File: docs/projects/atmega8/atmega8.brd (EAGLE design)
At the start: 89.8 x 49.5 mm, 13 parts, among them IC2 MEGA8-P

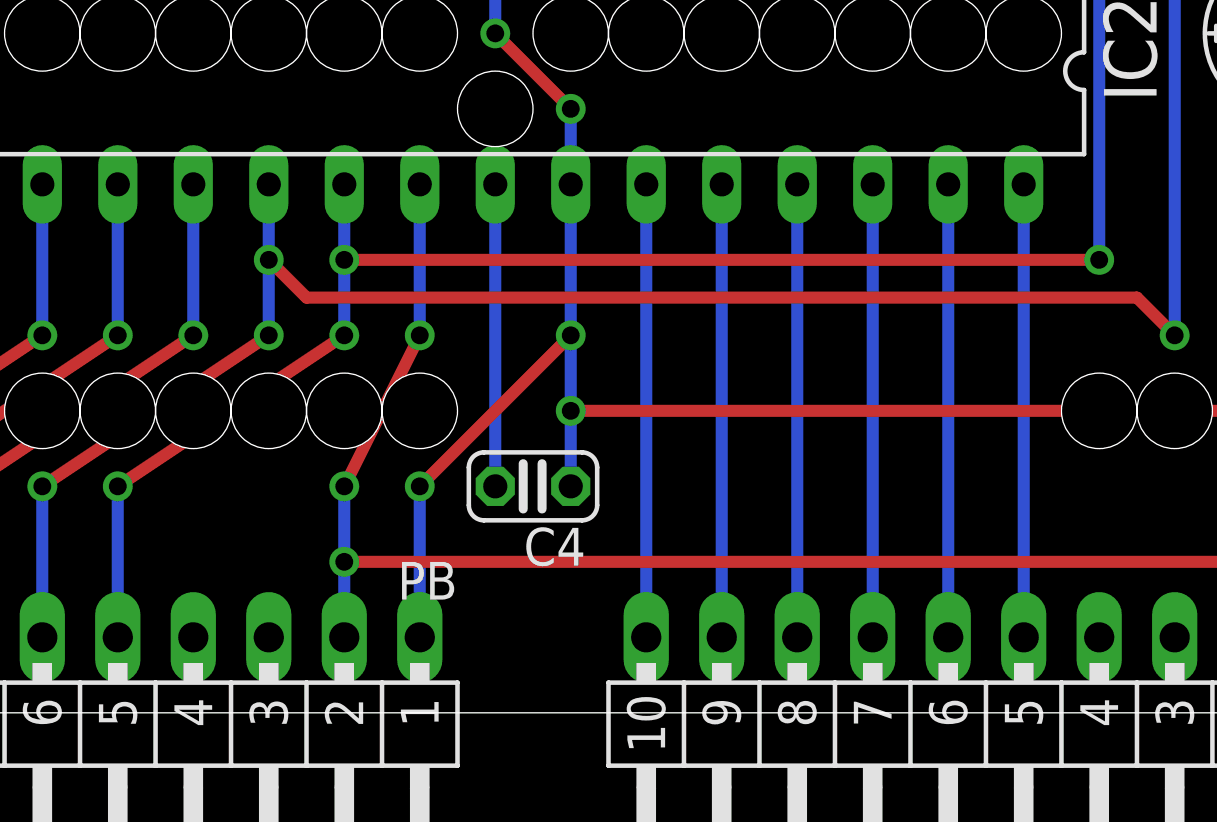
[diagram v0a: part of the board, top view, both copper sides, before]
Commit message: atmega8: 6,7 is connected with 14,15 to make I2C compatible with Nucleo
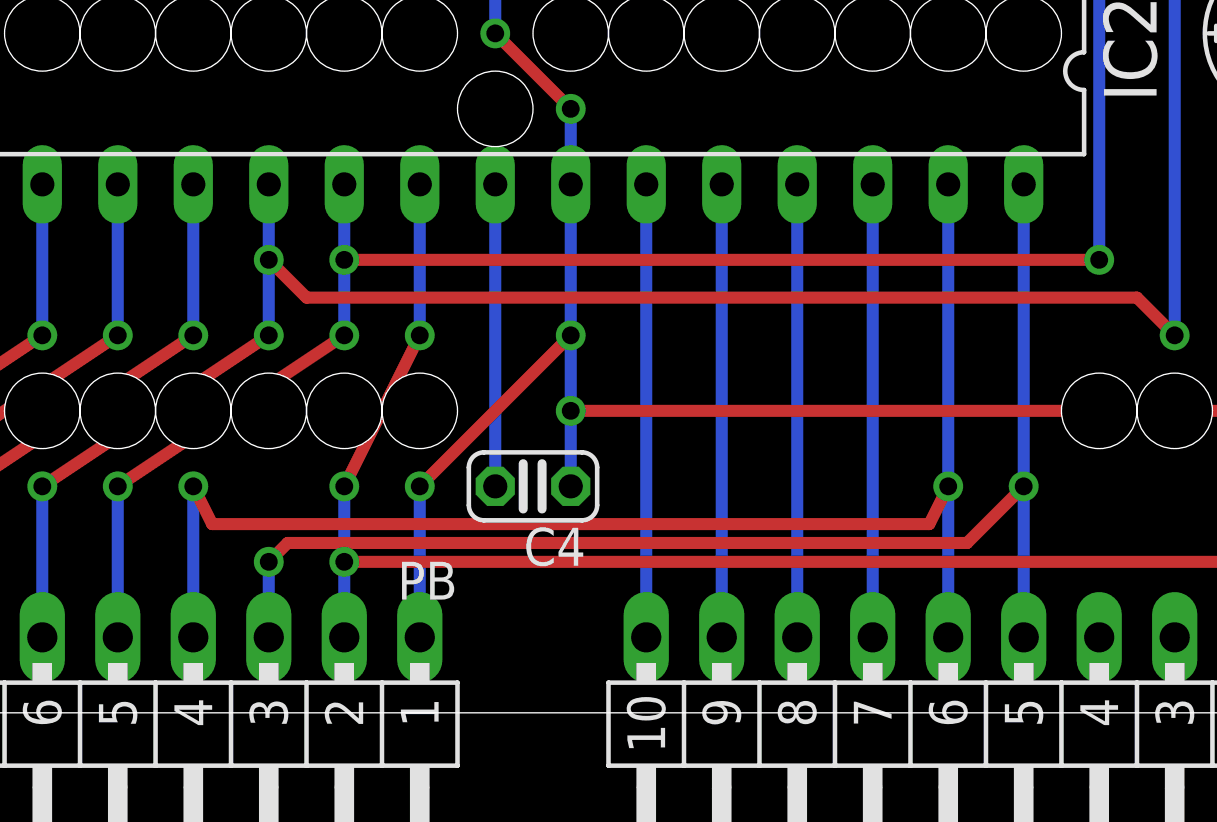
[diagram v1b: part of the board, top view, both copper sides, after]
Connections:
- removed net N$7: IC2.27, PC.6
- removed net N$8: IC2.28, PC.5
- new net A4: IC2.27, PB.4, PC.6
- new net A5: IC2.28, PB.3, PC.5
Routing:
- net A4: track 0.00 -> 47.3 mm, vias 0 -> 2
- net A5: track 0.00 -> 44.2 mm, vias 0 -> 2
- net N$8: track 15.2 -> 0.00 mm
- net N$7: track 15.2 -> 0.00 mm
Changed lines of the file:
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@@
 <?xml version="1.0" encoding="utf-8"?>
 <!DOCTYPE eagle SYSTEM "eagle.dtd">
-<eagle version="6.2">
+<eagle version="7.4.0">
 <drawing>
 <settings>
@@
 <setting verticaltext="up"/>
 </settings>
-<grid distance="0.1" unitdist="inch" unit="inch" style="lines" multiple="1" display="yes" altdistance="0.05" altunitdist="inch" altunit="inch"/>
+<grid distance="0.1" unitdist="inch" unit="inch" style="lines" multiple="1" display="yes" altdistance="0.025" altunitdist="inch" altunit="inch"/>
 <layers>
 <layer number="1" name="Top" color="4" fill="1" visible="yes" active="yes"/>
@@
 </class>
 </classes>
-<designrules>
+<designrules name="default">
 <description language="de">&lt;b&gt;EAGLE Design Rules&lt;/b&gt;
 &lt;p&gt;
@@
 <pass name="Default">
 <param name="RoutingGrid" value="50mil"/>
+<param name="AutoGrid" value="1"/>
+<param name="Efforts" value="0"/>
+<param name="TopRouterVariant" value="1"/>
 <param name="tpViaShape" value="round"/>
 <param name="PrefDir.1" value="|"/>
@@
 <wire x1="40.64" y1="2.54" x2="40.64" y2="17.78" width="0.4064" layer="16"/>
 </signal>
-<signal name="N$7">
+<signal name="A4">
 <contactref element="PC" pad="6"/>
 <contactref element="IC2" pad="27"/>
-<wire x1="43.18" y1="2.54" x2="43.18" y2="17.78" width="0.4064" layer="16"/>
-</signal>
-<signal name="N$8">
+<contactref element="PB" pad="4"/>
+<wire x1="43.18" y1="7.62" x2="43.18" y2="17.78" width="0.4064" layer="16"/>
+<wire x1="43.18" y1="2.54" x2="43.18" y2="7.62" width="0.4064" layer="16"/>
+<via x="43.18" y="7.62" extent="1-16" drill="0.6" shape="square"/>
+<wire x1="43.18" y1="7.62" x2="42.545" y2="6.35" width="0.4064" layer="1"/>
+<wire x1="42.545" y1="6.35" x2="18.415" y2="6.35" width="0.4064" layer="1"/>
+<wire x1="18.415" y1="6.35" x2="17.78" y2="7.62" width="0.4064" layer="1"/>
+<via x="17.78" y="7.62" extent="1-16" drill="0.6" shape="square"/>
+<wire x1="17.78" y1="7.62" x2="17.78" y2="2.54" width="0.4064" layer="16"/>
+</signal>
+<signal name="A5">
 <contactref element="PC" pad="5"/>
 <contactref element="IC2" pad="28"/>
-<wire x1="45.72" y1="2.54" x2="45.72" y2="17.78" width="0.4064" layer="16"/>
+<contactref element="PB" pad="3"/>
+<wire x1="45.72" y1="7.62" x2="45.72" y2="17.78" width="0.4064" layer="16"/>
+<wire x1="45.72" y1="2.54" x2="45.72" y2="7.62" width="0.4064" layer="16"/>
+<via x="45.72" y="7.62" extent="1-16" drill="0.6" shape="square"/>
+<wire x1="45.72" y1="7.62" x2="43.815" y2="5.715" width="0.4064" layer="1"/>
+<via x="20.32" y="5.08" extent="1-16" drill="0.6" shape="square"/>
+<wire x1="20.32" y1="5.08" x2="20.32" y2="2.54" width="0.4064" layer="16"/>
+<wire x1="43.815" y1="5.715" x2="20.955" y2="5.715" width="0.4064" layer="1"/>
+<wire x1="20.955" y1="5.715" x2="20.32" y2="5.08" width="0.4064" layer="1"/>
 </signal>
 <signal name="RXD">
